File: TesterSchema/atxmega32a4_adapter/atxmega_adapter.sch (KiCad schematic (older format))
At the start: 23 parts, among them IC1 ATXMEGA32A4-M, P1 DIL40, Q1 BC817-40, Q2 BC817-40, Q3 BC817-40

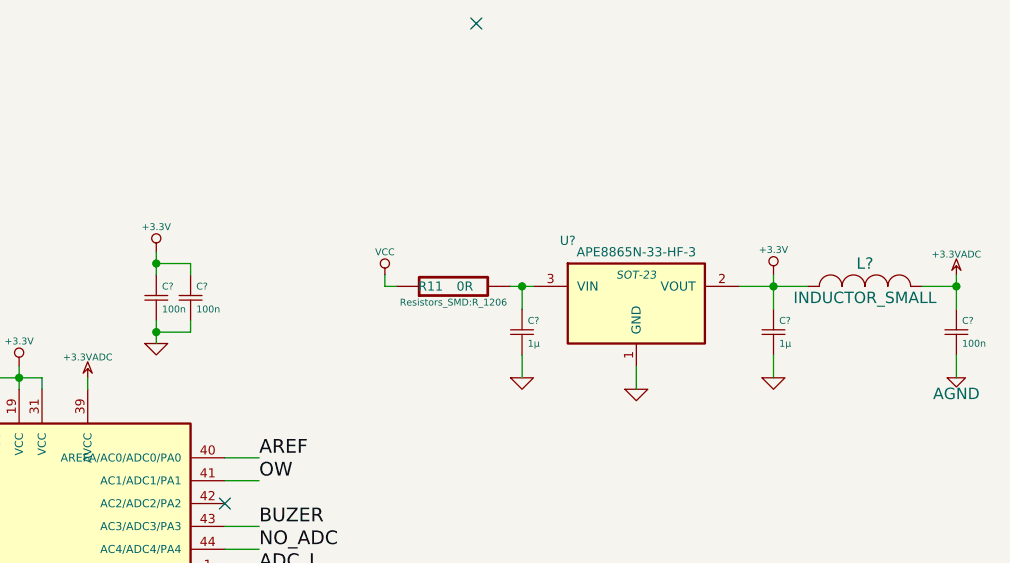
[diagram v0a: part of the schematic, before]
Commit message: Poprawa schematu płytki
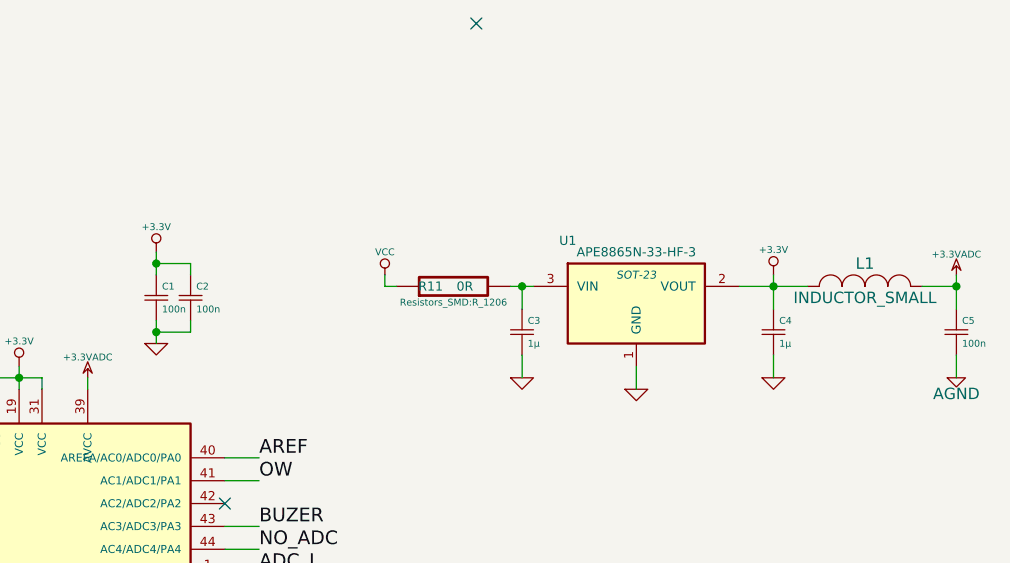
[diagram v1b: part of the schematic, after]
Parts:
- gave numbers to parts that had none: 7
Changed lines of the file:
@@
 $EndComp
 $Comp
-L +3.3V #PWR01
+L +3.3V #PWR11
 U 1 1 530289A6
 P 4500 1150
-F 0 "#PWR01" H 4500 1110 30  0001 C CNN
+F 0 "#PWR11" H 4500 1110 30  0001 C CNN
 F 1 "+3.3V" H 4500 1260 30  0000 C CNN
 F 2 "" H 4500 1150 60  0000 C CNN
@@
 $EndComp
 $Comp
-L GND #PWR02
+L GND #PWR5
 U 1 1 5303D961
 P 2250 2650
-F 0 "#PWR02" H 2250 2650 30  0001 C CNN
+F 0 "#PWR5" H 2250 2650 30  0001 C CNN
 F 1 "GND" H 2250 2580 30  0001 C CNN
 F 2 "" H 2250 2650 60  0000 C CNN
@@
 $EndComp
 $Comp
-L GND #PWR03
+L GND #PWR10
 U 1 1 5303E95D
 P 4350 3950
-F 0 "#PWR03" H 4350 3950 30  0001 C CNN
+F 0 "#PWR10" H 4350 3950 30  0001 C CNN
 F 1 "GND" H 4350 3880 30  0001 C CNN
 F 2 "" H 4350 3950 60  0000 C CNN
@@
 $EndComp
 $Comp
-L GND #PWR04
+L GND #PWR9
 U 1 1 5303EC6F
 P 3950 5550
-F 0 "#PWR04" H 3950 5550 30  0001 C CNN
+F 0 "#PWR9" H 3950 5550 30  0001 C CNN
 F 1 "GND" H 3950 5480 30  0001 C CNN
 F 2 "" H 3950 5550 60  0000 C CNN
@@
 $EndComp
 $Comp
-L VCC #PWR05
+L VCC #PWR8
 U 1 1 5303EDF7
 P 3950 5450
-F 0 "#PWR05" H 3950 5550 30  0001 C CNN
+F 0 "#PWR8" H 3950 5550 30  0001 C CNN
 F 1 "VCC" H 3950 5550 30  0000 C CNN
 F 2 "" H 3950 5450 60  0000 C CNN
@@
 $EndComp
 $Comp
-L AGND #PWR06
+L AGND #PWR16
 U 1 1 5303EF26
 P 5200 5450
-F 0 "#PWR06" H 5200 5450 40  0001 C CNN
+F 0 "#PWR16" H 5200 5450 40  0001 C CNN
 F 1 "AGND" H 5200 5380 50  0000 C CNN
 F 2 "" H 5200 5450 60  0000 C CNN
@@
 $EndComp
 $Comp
-L AGND #PWR07
+L AGND #PWR12
 U 1 1 5303F466
 P 4650 3950
-F 0 "#PWR07" H 4650 3950 40  0001 C CNN
+F 0 "#PWR12" H 4650 3950 40  0001 C CNN
 F 1 "AGND" H 4650 3880 50  0000 C CNN
 F 2 "" H 4650 3950 60  0000 C CNN
@@
 XTAL2
 $Comp
-L +3.3V #PWR08
+L +3.3V #PWR14
 U 1 1 5304022C
 P 5100 650
-F 0 "#PWR08" H 5100 610 30  0001 C CNN
+F 0 "#PWR14" H 5100 610 30  0001 C CNN
 F 1 "+3.3V" H 5100 760 30  0000 C CNN
 F 2 "" H 5100 650 60  0000 C CNN
@@
 $EndComp
 $Comp
-L GND #PWR09
+L GND #PWR15
 U 1 1 53040959
 P 5100 1050
-F 0 "#PWR09" H 5100 1050 30  0001 C CNN
+F 0 "#PWR15" H 5100 1050 30  0001 C CNN
 F 1 "GND" H 5100 980 30  0001 C CNN
 F 2 "" H 5100 1050 60  0000 C CNN
@@
 $EndComp
 $Comp
-L GND #PWR010
+L GND #PWR4
 U 1 1 530499C3
 P 2100 2400
-F 0 "#PWR010" H 2100 2400 30  0001 C CNN
+F 0 "#PWR4" H 2100 2400 30  0001 C CNN
 F 1 "GND" H 2100 2330 30  0001 C CNN
 F 2 "" H 2100 2400 60  0000 C CNN
@@
 $EndComp
 $Comp
-L GND #PWR011
+L GND #PWR3
 U 1 1 5304A14A
 P 2100 1700
-F 0 "#PWR011" H 2100 1700 30  0001 C CNN
+F 0 "#PWR3" H 2100 1700 30  0001 C CNN
 F 1 "GND" H 2100 1630 30  0001 C CNN
 F 2 "" H 2100 1700 60  0000 C CNN
@@
 $EndComp
 $Comp
-L VCC #PWR012
+L VCC #PWR6
 U 1 1 5304A6D2
 P 3000 1100
-F 0 "#PWR012" H 3000 1200 30  0001 C CNN
+F 0 "#PWR6" H 3000 1200 30  0001 C CNN
 F 1 "VCC" H 3000 1200 30  0000 C CNN
 F 2 "" H 3000 1100 60  0000 C CNN
@@
 $EndComp
 $Comp
-L VCC #PWR013
+L VCC #PWR7
 U 1 1 5304B555
 P 3000 1800
-F 0 "#PWR013" H 3000 1900 30  0001 C CNN
+F 0 "#PWR7" H 3000 1900 30  0001 C CNN
 F 1 "VCC" H 3000 1900 30  0000 C CNN
 F 2 "" H 3000 1800 60  0000 C CNN
@@
 $EndComp
 $Comp
-L GND #PWR014
+L GND #PWR2
 U 1 1 530511DC
 P 1800 3200
-F 0 "#PWR014" H 1800 3200 30  0001 C CNN
+F 0 "#PWR2" H 1800 3200 30  0001 C CNN
 F 1 "GND" H 1800 3130 30  0001 C CNN
 F 2 "" H 1800 3200 60  0000 C CNN
@@
 $EndComp
 $Comp
-L VCC #PWR015
+L VCC #PWR1
 U 1 1 53051256
 P 1800 2050
-F 0 "#PWR015" H 1800 2150 30  0001 C CNN
+F 0 "#PWR1" H 1800 2150 30  0001 C CNN
 F 1 "VCC" H 1800 2150 30  0000 C CNN
 F 2 "" H 1800 2050 60  0000 C CNN
@@
 SW3
 $Comp
-L GND #PWR016
+L GND #PWR18
 U 1 1 53051A5D
 P 6700 1200
-F 0 "#PWR016" H 6700 1200 30  0001 C CNN
+F 0 "#PWR18" H 6700 1200 30  0001 C CNN
 F 1 "GND" H 6700 1130 30  0001 C CNN
 F 2 "" H 6700 1200 60  0000 C CNN
@@
 $EndComp
 $Comp
-L GND #PWR017
+L GND #PWR19
 U 1 1 53051AD3
 P 7200 1250
-F 0 "#PWR017" H 7200 1250 30  0001 C CNN
+F 0 "#PWR19" H 7200 1250 30  0001 C CNN
 F 1 "GND" H 7200 1180 30  0001 C CNN
 F 2 "" H 7200 1250 60  0000 C CNN
@@
 $EndComp
 $Comp
-L GND #PWR018
+L GND #PWR21
 U 1 1 53051AD9
 P 7800 1200
-F 0 "#PWR018" H 7800 1200 30  0001 C CNN
+F 0 "#PWR21" H 7800 1200 30  0001 C CNN
 F 1 "GND" H 7800 1130 30  0001 C CNN
 F 2 "" H 7800 1200 60  0000 C CNN
@@
 $EndComp
 $Comp
-L VCC #PWR019
+L VCC #PWR17
 U 1 1 53051C38
 P 6100 750
-F 0 "#PWR019" H 6100 850 30  0001 C CNN
+F 0 "#PWR17" H 6100 850 30  0001 C CNN
 F 1 "VCC" H 6100 850 30  0000 C CNN
 F 2 "" H 6100 750 60  0000 C CNN
@@
 $EndComp
 $Comp
-L +3.3V #PWR020
+L +3.3V #PWR20
 U 1 1 53051C45
 P 7800 750
-F 0 "#PWR020" H 7800 710 30  0001 C CNN
+F 0 "#PWR20" H 7800 710 30  0001 C CNN
 F 1 "+3.3V" H 7800 860 30  0000 C CNN
 F 2 "" H 7800 750 60  0000 C CNN
@@
 NoConn ~ 4850 5550
 $Comp
-L +3.3VADC #PWR021
+L +3.3VADC #PWR22
 U 1 1 53051F97
 P 8600 750
-F 0 "#PWR021" H 8600 870 20  0001 C CNN
+F 0 "#PWR22" H 8600 870 20  0001 C CNN
 F 1 "+3.3VADC" H 8600 840 30  0000 C CNN
 F 2 "" H 8600 750 60  0000 C CNN
@@
 $EndComp
 $Comp
-L +3.3VADC #PWR022
+L +3.3VADC #PWR13
 U 1 1 5305201B
 P 4800 1200
-F 0 "#PWR022" H 4800 1320 20  0001 C CNN
+F 0 "#PWR13" H 4800 1320 20  0001 C CNN
 F 1 "+3.3VADC" H 4800 1290 30  0000 C CNN
 F 2 "" H 4800 1200 60  0000 C CNN
@@
 SW4
 $Comp
-L AGND #PWR023
+L AGND #PWR23
 U 1 1 530527D7
 P 8600 1200
-F 0 "#PWR023" H 8600 1200 40  0001 C CNN
+F 0 "#PWR23" H 8600 1200 40  0001 C CNN
 F 1 "AGND" H 8600 1130 50  0000 C CNN
 F 2 "" H 8600 1200 60  0000 C CNN
@@
 NoConn ~ 3600 3150
 $Comp
-L Csmall C?
+L Csmall C1
 U 1 1 54D13C7F
 P 5100 850
-F 0 "C?" H 5125 900 30  0000 L CNN
+F 0 "C1" H 5125 900 30  0000 L CNN
 F 1 "100n" H 5125 800 30  0000 L CNN
 F 2 "" H 5100 850 60  0000 C CNN
@@
 $EndComp
 $Comp
-L Csmall C?
+L Csmall C2
 U 1 1 54D13CD2
 P 5250 850
-F 0 "C?" H 5275 900 30  0000 L CNN
+F 0 "C2" H 5275 900 30  0000 L CNN
 F 1 "100n" H 5275 800 30  0000 L CNN
 F 2 "" H 5250 850 60  0000 C CNN
@@
 $EndComp
 $Comp
-L Csmall C?
+L Csmall C3
 U 1 1 54D13F35
 P 6700 1000
-F 0 "C?" H 6725 1050 30  0000 L CNN
+F 0 "C3" H 6725 1050 30  0000 L CNN
 F 1 "1µ" H 6725 950 30  0000 L CNN
 F 2 "" H 6700 1000 60  0000 C CNN
@@
 $EndComp
 $Comp
-L Csmall C?
+L Csmall C4
 U 1 1 54D1410B
 P 7800 1000
-F 0 "C?" H 7825 1050 30  0000 L CNN
+F 0 "C4" H 7825 1050 30  0000 L CNN
 F 1 "1µ" H 7825 950 30  0000 L CNN
 F 2 "" H 7800 1000 60  0000 C CNN
@@
 $EndComp
 $Comp
-L Csmall C?
+L Csmall C5
 U 1 1 54D1423D
 P 8600 1000
-F 0 "C?" H 8625 1050 30  0000 L CNN
+F 0 "C5" H 8625 1050 30  0000 L CNN
 F 1 "100n" H 8625 950 30  0000 L CNN
 F 2 "" H 8600 1000 60  0000 C CNN
@@
 $EndComp
 $Comp
-L INDUCTOR_SMALL L?
+L INDUCTOR_SMALL L1
 U 1 1 54D1443A
 P 8200 800
-F 0 "L?" H 8200 900 50  0000 C CNN
+F 0 "L1" H 8200 900 50  0000 C CNN
 F 1 "INDUCTOR_SMALL" H 8200 750 50  0000 C CNN
 F 2 "" H 8200 800 60  0000 C CNN
@@
 $EndComp
 $Comp
-L APE8865N-33-HF-3 U?
+L APE8865N-33-HF-3 U1
 U 1 1 54D1474B
 P 7200 850
-F 0 "U?" H 6900 1100 40  0000 C CNN
+F 0 "U1" H 6900 1100 40  0000 C CNN
 F 1 "APE8865N-33-HF-3" H 7200 1050 40  0000 C CNN
 F 2 "SOT-23" H 7200 950 35  0000 C CIN

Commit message: zmiany z adapterze
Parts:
- C1, C2, C5: footprint (none) -> Capacitors_SMD:C_0603_HandSoldering
- C3, C4: footprint (none) -> Capacitors_SMD:C_1206_HandSoldering
- L1: footprint (none) -> Choke_SMD:Choke_SMD_1206_Handsoldering
- U1: footprint SOT-23 -> SMD_Packages:SOT-23
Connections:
- wire segments 119 -> 133
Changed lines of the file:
@@
 SW3
-$Comp
-L GND #PWR18
-U 1 1 53051A5D
-P 6700 1200
-F 0 "#PWR18" H 6700 1200 30  0001 C CNN
-F 1 "GND" H 6700 1130 30  0001 C CNN
-F 2 "" H 6700 1200 60  0000 C CNN
-F 3 "" H 6700 1200 60  0000 C CNN
-	1    6700 1200
-	1    0    0    -1
-$EndComp
-$Comp
-L GND #PWR19
-U 1 1 53051AD3
-P 7200 1250
-F 0 "#PWR19" H 7200 1250 30  0001 C CNN
-F 1 "GND" H 7200 1180 30  0001 C CNN
-F 2 "" H 7200 1250 60  0000 C CNN
-F 3 "" H 7200 1250 60  0000 C CNN
-	1    7200 1250
-	1    0    0    -1
-$EndComp
-$Comp
-L GND #PWR21
-U 1 1 53051AD9
-P 7800 1200
-F 0 "#PWR21" H 7800 1200 30  0001 C CNN
-F 1 "GND" H 7800 1130 30  0001 C CNN
-F 2 "" H 7800 1200 60  0000 C CNN
-F 3 "" H 7800 1200 60  0000 C CNN
-	1    7800 1200
-	1    0    0    -1
-$EndComp
 $Comp
 L VCC #PWR17
@@
 L AGND #PWR23
 U 1 1 530527D7
-P 8600 1200
-F 0 "#PWR23" H 8600 1200 40  0001 C CNN
-F 1 "AGND" H 8600 1130 50  0000 C CNN
-F 2 "" H 8600 1200 60  0000 C CNN
-F 3 "" H 8600 1200 60  0000 C CNN
-	1    8600 1200
+P 8600 1250
+F 0 "#PWR23" H 8600 1250 40  0001 C CNN
+F 1 "AGND" H 8600 1180 50  0000 C CNN
+F 2 "" H 8600 1250 60  0000 C CNN
+F 3 "" H 8600 1250 60  0000 C CNN
+	1    8600 1250
 	1    0    0    -1
 $EndComp
@@
 NoConn ~ 5400 1750
 Wire Wire Line
-	4350 3850 4350 3950
-Wire Wire Line
-	4500 1150 4500 1250
+	4350 3850 4350 3900
+Wire Wire Line
+	4350 3900 4350 3950
+Wire Wire Line
+	4500 1150 4500 1200
+Wire Wire Line
+	4500 1200 4500 1250
 Wire Wire Line
 	3950 4950 4150 4950
@@
 	2950 2700 3600 2700
 Wire Wire Line
-	2950 2600 3600 2600
+	2950 2600 3000 2600
+Wire Wire Line
+	3000 2600 3600 2600
 Connection ~ 3000 2600
 Wire Wire Line
@@
 	3000 2500 3000 2600
 Wire Wire Line
-	4350 3900 4550 3900
+	4350 3900 4450 3900
+Wire Wire Line
+	4450 3900 4550 3900
 Wire Wire Line
 	4550 3900 4550 3850
@@
 	4400 1250 4400 1200
 Wire Wire Line
-	4400 1200 4600 1200
+	4400 1200 4500 1200
+Wire Wire Line
+	4500 1200 4600 1200
 Connection ~ 4500 1200
 Wire Wire Line
@@
 	3500 2150 3600 2150
 Wire Wire Line
-	5100 650  5100 750
+	5100 650  5100 700
+Wire Wire Line
+	5100 700  5100 750
 Wire Wire Line
 	5250 700  5250 750
 Connection ~ 5100 700
 Wire Wire Line
-	5100 950  5100 1050
+	5100 950  5100 1000
+Wire Wire Line
+	5100 1000 5100 1050
 Wire Wire Line
 	5250 950  5250 1000
 Connection ~ 5100 1000
 Wire Wire Line
-	1850 1900 2450 1900
-Wire Wire Line
-	1850 1200 2450 1200
+	1850 1900 2100 1900
+Wire Wire Line
+	2100 1900 2450 1900
+Wire Wire Line
+	1850 1200 2100 1200
+Wire Wire Line
+	2100 1200 2450 1200
 Wire Wire Line
 	2100 2350 2100 2400
@@
 	1600 2650 1800 2650
 Wire Wire Line
-	1800 2600 1800 2700
+	1800 2600 1800 2650
+Wire Wire Line
+	1800 2650 1800 2700
 Wire Wire Line
 	2450 2700 2400 2700
@@
 	5400 2600 5550 2600
 Wire Wire Line
-	7650 800  7950 800
-Wire Wire Line
-	7800 750  7800 900
-Wire Wire Line
-	6700 1100 6700 1200
+	7650 800  7800 800
+Wire Wire Line
+	7800 800  7950 800
+Wire Wire Line
+	7800 750  7800 800
+Wire Wire Line
+	7800 800  7800 900
+Wire Wire Line
+	6700 1100 6700 1250
 Wire Wire Line
 	7200 1150 7200 1250
 Wire Wire Line
-	7800 1100 7800 1200
+	7800 1100 7800 1250
 Connection ~ 7800 800
 Wire Wire Line
 	8450 800  8600 800
 Wire Wire Line
-	8600 750  8600 900
-Wire Wire Line
-	8600 1100 8600 1200
+	8600 750  8600 800
+Wire Wire Line
+	8600 800  8600 900
+Wire Wire Line
+	8600 1100 8600 1250
 Connection ~ 8600 800
 Wire Wire Line
@@
 F 0 "C1" H 5125 900 30  0000 L CNN
 F 1 "100n" H 5125 800 30  0000 L CNN
-F 2 "" H 5100 850 60  0000 C CNN
+F 2 "Capacitors_SMD:C_0603_HandSoldering" H 5100 850 60  0001 C CNN
 F 3 "" H 5100 850 60  0000 C CNN
 	1    5100 850
@@
 F 0 "C2" H 5275 900 30  0000 L CNN
 F 1 "100n" H 5275 800 30  0000 L CNN
-F 2 "" H 5250 850 60  0000 C CNN
+F 2 "Capacitors_SMD:C_0603_HandSoldering" H 5250 850 60  0001 C CNN
 F 3 "" H 5250 850 60  0000 C CNN
 	1    5250 850
@@
 F 0 "C3" H 6725 1050 30  0000 L CNN
 F 1 "1µ" H 6725 950 30  0000 L CNN
-F 2 "" H 6700 1000 60  0000 C CNN
+F 2 "Capacitors_SMD:C_1206_HandSoldering" H 6700 1000 60  0001 C CNN
 F 3 "" H 6700 1000 60  0000 C CNN
 	1    6700 1000
@@
 F 0 "C4" H 7825 1050 30  0000 L CNN
 F 1 "1µ" H 7825 950 30  0000 L CNN
-F 2 "" H 7800 1000 60  0000 C CNN
+F 2 "Capacitors_SMD:C_1206_HandSoldering" H 7800 1000 60  0001 C CNN
 F 3 "" H 7800 1000 60  0000 C CNN
 	1    7800 1000
@@
 F 0 "C5" H 8625 1050 30  0000 L CNN
 F 1 "100n" H 8625 950 30  0000 L CNN
-F 2 "" H 8600 1000 60  0000 C CNN
+F 2 "Capacitors_SMD:C_0603_HandSoldering" H 8600 1000 60  0001 C CNN
 F 3 "" H 8600 1000 60  0000 C CNN
 	1    8600 1000
@@
 F 0 "L1" H 8200 900 50  0000 C CNN
 F 1 "INDUCTOR_SMALL" H 8200 750 50  0000 C CNN
-F 2 "" H 8200 800 60  0000 C CNN
+F 2 "Choke_SMD:Choke_SMD_1206_Handsoldering" H 8200 800 60  0001 C CNN
 F 3 "" H 8200 800 60  0000 C CNN
 	1    8200 800
@@
 F 0 "U1" H 6900 1100 40  0000 C CNN
 F 1 "APE8865N-33-HF-3" H 7200 1050 40  0000 C CNN
-F 2 "SOT-23" H 7200 950 35  0000 C CIN
+F 2 "SMD_Packages:SOT-23" H 7200 950 35  0000 C CIN
 F 3 "" H 7200 850 60  0000 C CNN
 	1    7200 850
@@
 $EndComp
 Wire Wire Line
-	6650 800  6750 800
+	6650 800  6700 800
+Wire Wire Line
+	6700 800  6750 800
 Wire Wire Line
 	6700 800  6700 900
 Connection ~ 6700 800
+$Comp
+L GND #PWR18
+U 1 1 53051A5D
+P 6700 1250
+F 0 "#PWR18" H 6700 1250 30  0001 C CNN
+F 1 "GND" H 6700 1180 30  0001 C CNN
+F 2 "" H 6700 1250 60  0000 C CNN
+F 3 "" H 6700 1250 60  0000 C CNN
+	1    6700 1250
+	1    0    0    -1
+$EndComp
+$Comp
+L GND #PWR19
+U 1 1 53051AD3
+P 7200 1250
+F 0 "#PWR19" H 7200 1250 30  0001 C CNN
+F 1 "GND" H 7200 1180 30  0001 C CNN
+F 2 "" H 7200 1250 60  0000 C CNN
+F 3 "" H 7200 1250 60  0000 C CNN
+	1    7200 1250
+	1    0    0    -1
+$EndComp
+$Comp
+L GND #PWR21
+U 1 1 53051AD9
+P 7800 1250
+F 0 "#PWR21" H 7800 1250 30  0001 C CNN
+F 1 "GND" H 7800 1180 30  0001 C CNN
+F 2 "" H 7800 1250 60  0000 C CNN
+F 3 "" H 7800 1250 60  0000 C CNN
+	1    7800 1250
+	1    0    0    -1
+$EndComp
 $EndSCHEMATC
